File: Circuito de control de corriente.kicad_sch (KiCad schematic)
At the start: 24 parts, among them K1 JJM1-12V, K2 JJM1-12V, K3 JJM1-12V, U18 IRLZ44N, U20 IRLZ44N, U22 IRLZ44N, U3 A6841, U55 IRLZ44N

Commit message: Version V1 (Clearence + pads)
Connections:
- no-connect marks 8 -> 11
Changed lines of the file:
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@@
   )
   (no_connect (at 38.1 107.95))
+  (no_connect (at 143.51 157.48))
+  (no_connect (at 143.51 154.94))
+  (no_connect (at 105.41 152.4))
   (no_connect (at 40.64 107.95))
   (no_connect (at 247.65 106.68))

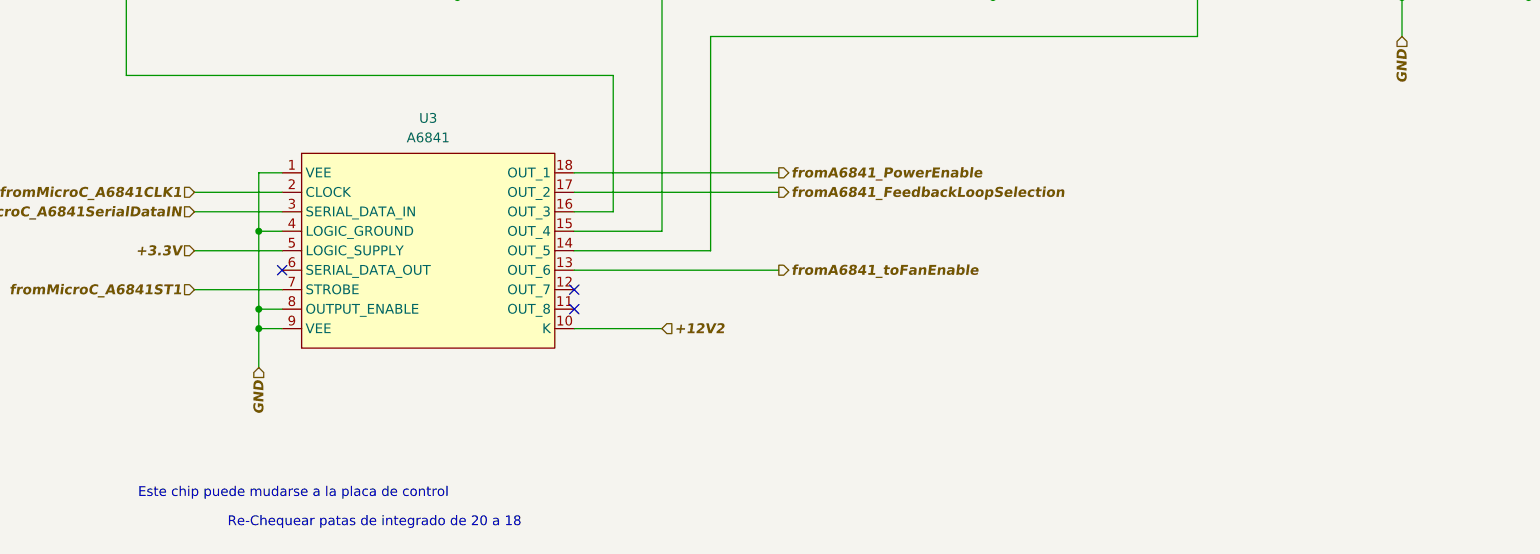
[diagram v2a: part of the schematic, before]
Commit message: Heat sink added + Large pads
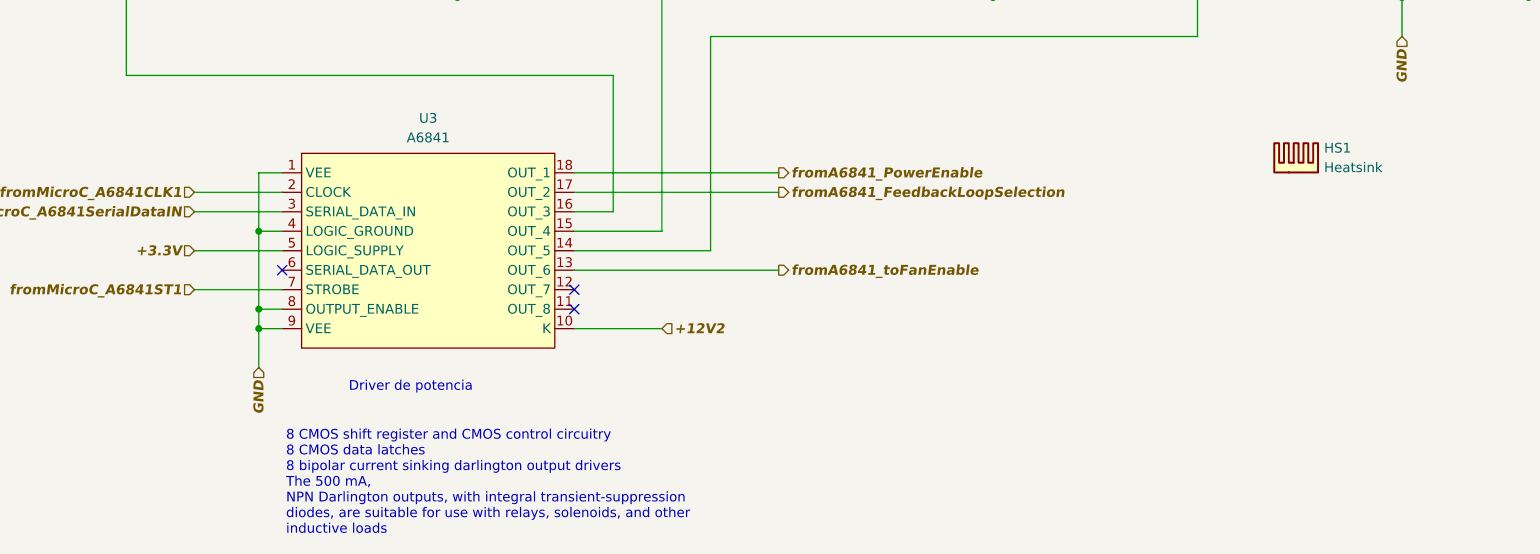
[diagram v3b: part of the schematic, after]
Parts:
- added HS1: Heatsink, Heatsink:Heatsink_125x35x50mm_3xFixationM3, symbol Mechanical:Heatsink
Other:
- note added: "8 CMOS shift register and CMOS control circuitry 8 CMOS data latches 8 bipolar current sinking darlington output drivers The 500 mA, NPN Darlington outputs, with integral transient-suppression diodes, are suitable for use with relays, solenoids, and other inductive loads"
- note added: "Driver de potencia"
- note removed: "Este chip puede mudarse a la placa de control"
- note removed: "Re-Chequear patas de integrado de 20 a 18"
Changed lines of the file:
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@@
     (stroke (width 0) (type default) (color 0 0 0 0))
+  )
+  (text "Driver de potencia" (at 114.0968 168.402 0)
+    (effects (font (size 1.27 1.27)) (justify left bottom))
+  )
+  (text "8 CMOS shift register and CMOS control circuitry\n8 CMOS data latches\n8 bipolar current sinking darlington output drivers\nThe 500 mA,\nNPN Darlington outputs, with integral transient-suppression\ndiodes, are suitable for use with relays, solenoids, and other\ninductive loads\n"
+    (at 105.918 187.0456 0)
+    (effects (font (size 1.27 1.27)) (justify left bottom))
   )
   (text "Circuito de control de corriente" (at 33.274 29.845 0)
     (effects (font (size 3.5 3.5) (thickness 0.5994) bold) (justify left bottom))
-  )
-  (text "Este chip puede mudarse a la placa de control" (at 86.614 182.245 0)
-    (effects (font (size 1.27 1.27)) (justify left bottom))
   )
   (text "Las resistencias R10, R20, \nR40 y R40 de 22 Ohm deberia \nser de 1W"
     (at 21.59 129.54 0)
     (effects (font (size 1.27 1.27) (thickness 0.254) bold) (justify left bottom))
-  )
-  (text "Re-Chequear patas de integrado de 20 a 18\n" (at 98.298 186.055 0)
-    (effects (font (size 1.27 1.27)) (justify left bottom))
   )
   (label "GS2" (at 118.11 72.39 0)
@@
     (pin "2")
   )
+  (symbol (lib_id "Mechanical:Heatsink") (at 237.6678 139.6492 0) (unit 1)
+    (in_bom yes) (on_board yes) (fields_autoplaced)
+    (property "Reference" "HS1" (id 0) (at 241.3 136.4741 0)
+      (effects (font (size 1.27 1.27)) (justify left))
+    )
+    (property "Value" "Heatsink" (id 1) (at 241.3 139.0141 0)
+      (effects (font (size 1.27 1.27)) (justify left))
+    )
+    (property "Footprint" "Heatsink:Heatsink_125x35x50mm_3xFixationM3" (id 2) (at 237.9726 139.6492 0)
+      (effects (font (size 1.27 1.27)) hide)
+    )
+    (property "Datasheet" "~" (id 3) (at 237.9726 139.6492 0)
+      (effects (font (size 1.27 1.27)) hide)
+    )
+  )
   (symbol (lib_id "Device:R_Small") (at 172.085 72.39 90) (unit 1)

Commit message: Pads mas grandes y correccion de vias
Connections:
- net PushPullOUT: now also K1.3 (NC), K2.3 (NC), K3.3 (NC); no longer K1.5 (C), K2.5 (C), K3.5 (C)
- net at R13.1: now also K3.5 (C); no longer K3.3 (NO)
- net at R10.1: now also K1.5 (C); no longer K1.3 (NO)
- net at R12.1: now also K2.5 (C); no longer K2.3 (NO)
- net CEP_Input+ renamed CEP_Input+_MOS

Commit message: V4 Ltspice
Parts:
- removed UA2, UA3, UA4, UA5: LM311, CEDCp:LM311P, symbol Comparator:LM311
- added UA2, UA3, UA4, UA5: LM311_V2, CEDCp_V2:LM311_V2, symbol CEDCp_V2:LM311_V2
- R10: renamed from R8; footprint CEDCp:Resistencia_0,25W -> CEDCp_V2:Resistencia_0,25W
- R20: renamed from R10; footprint CEDCp:Resistencia_0,25W -> CEDCp_V2:Resistencia_0,25W
- R30: renamed from R12; footprint CEDCp:Resistencia_0,25W -> CEDCp_V2:Resistencia_0,25W
- R40: renamed from R13; footprint CEDCp:Resistencia_0,25W -> CEDCp_V2:Resistencia_0,25W
- ROp1, ROp2, ROp3, ROp4: footprint CEDCp:Resistencia_0,25W -> CEDCp_V2:Resistencia_0,25W
- renumbered R9 to R12, R11 to R22, R37 to R32, R14 to R42, U55 to U1, U18 to U2, U20 to U3, U22 to U4, U3 to UB1
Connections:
- net +12V1: now also UA2.8 (V+), UA3.8 (V+), UA4.8 (V+), UA5.8 (V+)
- net CEP_Input-: now also K1.3 (NO), K2.3 (NO), K3.3 (NO), UA2.1 (EOut), UA2.4 (V-), UA3.1 (EOut), UA3.4 (V-), UA4.1 (EOut), UA4.4 (V-), UA5.1 (EOut), UA5.4 (V-); no longer K1.4 (NO), K2.4 (NO), K3.4 (NO)
- net GS1: now also UA2.7 (COut)
- net GS2: now also UA3.7 (COut)
- net GS3: now also UA4.7 (COut)
- net GS4: now also UA5.7 (COut)
- net ILimit_Vref: now also UA2.2 (+), UA3.2 (+), UA4.2 (+), UA5.2 (+)
- net PushPullOUT: now also K1.4 (NC), K2.4 (NC), K3.4 (NC); no longer K1.3 (NC), K2.3 (NC), K3.3 (NC)
- net V01: now also UA2.3 (-)
- net V02: now also UA3.3 (-)
- net V03: now also UA4.3 (-)
- net V04: now also UA5.3 (-)
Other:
- note added: "En este diseño esta considerada la resistencias opcionales en las bases de los MOSFETS. En LTSPICE no estan consideradas."
